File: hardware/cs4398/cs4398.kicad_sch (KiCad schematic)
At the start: 54 parts, among them J1 USB_C_Receptacle_USB2.0_16P, Q1 Si2323DS, U1 CS4398, U2 STM32H750IBKx, U3 TPS65131RGE, U4 USB3300-EZK, U5 TPS7A8300, U7 TPS60151DRV, Y1 CSTCE12M

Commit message: sync 9.15
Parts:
- removed R5: 1.5k, Resistor_SMD:R_0402_1005Metric, symbol Device:R
- added C1, C20: 10u, Capacitor_SMD:C_0805_2012Metric, symbol Device:C_Small
- added C16, C18, C21, C46, C47, C51, C52, C55, C56, C59, C6, C60, C64, C65, C66, C67, C68, C7, C71, C72, C73, C74, C77, C78, C79, C8: 100n, Capacitor_SMD:C_0402_1005Metric, symbol Device:C_Small
- added C19, C53, C54: 100u, Capacitor_Tantalum_SMD:CP_EIA-3528-15_AVX-H, symbol Device:C_Polarized_Small_US
- added C23, C4: 33u, Capacitor_Tantalum_SMD:CP_EIA-3528-15_AVX-H, symbol Device:C_Polarized_Small_US
- added C35, C41, C61, C75, C76: 100n, Capacitor_SMD:C_0603_1608Metric, symbol Device:C_Small
- added C44, C45: 6800p, Capacitor_SMD:C_0402_1005Metric, symbol Device:C_Small
- added C48, C49: 18n, Capacitor_SMD:C_0402_1005Metric, symbol Device:C_Small
- added C57, C58: 4700p, Capacitor_SMD:C_0402_1005Metric, symbol Device:C_Small
- added C62, C63: 1800p, Capacitor_SMD:C_0805_2012Metric, symbol Device:C_Small
- added C69, C70: 22u, Capacitor_Tantalum_SMD:CP_EIA-3528-15_AVX-H, symbol Device:C_Polarized_Small_US
- added C80, C81: 2.2u, Capacitor_SMD:C_0402_1005Metric, symbol Device:C_Small
- added F1: 1A, Fuse:Fuse_0603_1608Metric, symbol Device:Polyfuse
- added J2: GH1.25-4P, Connector_JST:JST_GH_BM04B-GHS-TBT_1x04-1MP_P1.25mm_Vertical, symbol Connector_Generic_MountingPin:Conn_01x04_MountingPin
- added Q2, Q3: S9012, Package_TO_SOT_SMD:SOT-23, symbol Transistor_BJT:MMBTA94
- added Q4, Q5: S9013, Package_TO_SOT_SMD:SOT-23, symbol Transistor_BJT:SS8050
- added R1, R11, R12, R13, R14: 10K, Resistor_SMD:R_0402_1005Metric, symbol Device:R
- added R10, R9: 2k, Resistor_SMD:R_0402_1005Metric, symbol Device:R
- added R15, R16: 1.5K, Resistor_SMD:R_0402_1005Metric, symbol Device:R
- added R20, R22, R37, R44, R45: 10k, Resistor_SMD:R_0603_1608Metric, symbol Device:R
- added R23, R25: 1.6k, Resistor_SMD:R_0402_1005Metric, symbol Device:R
- added R24, R26: 620, Resistor_SMD:R_0402_1005Metric, symbol Device:R
- added R27, R28, R30, R32: 270, Resistor_SMD:R_0402_1005Metric, symbol Device:R
- added R29, R31: 680, Resistor_SMD:R_0402_1005Metric, symbol Device:R
- added R33, R34: 100, Resistor_SMD:R_0603_1608Metric, symbol Device:R
- added R35, R36: 1.2k, Resistor_SMD:R_0402_1005Metric, symbol Device:R
- added R38, R39: 4.7K, Resistor_SMD:R_0603_1608Metric, symbol Device:R
- added R40, R41: 100k, Resistor_SMD:R_0402_1005Metric, symbol Device:R
- added R42, R43: 560, Resistor_SMD:R_0402_1005Metric, symbol Device:R
- added R46: 10k, Resistor_SMD:R_0402_1005Metric, symbol Device:R
- added R7, R8: 5.1k, Resistor_SMD:R_0402_1005Metric, symbol Device:R
- added SW1, SW2, SW3, SW4: SW_Omron_B3FS, Button_Switch_SMD:SW_SPST_TS-1088-xR025, symbol Switch:SW_Omron_B3FS
- added U6: OPA1612AxD, Package_SON:WSON-8-1EP_3x3mm_P0.5mm_EP1.2x2mm_ThermalVias, symbol Amplifier_Operational:OPA1612AxD
- added Y2: CSTCE24M, Crystal:Resonator_SMD_Murata_CSTxExxV-3Pin_3.0x1.1mm, symbol Device:Crystal_GND2_Small
- C22: renamed from C13; footprint Capacitor_SMD:C_0402_1005Metric -> Capacitor_SMD:C_0805_2012Metric
- Y1: value CSTCE12M -> CSTCE24M
- renumbered C22 to C11, C11 to C12, C28 to C13, C21 to C14, C23 to C15, C24 to C17, C4 to C2, C7 to C24, C6 to C25, C12 to C26, C5 to C27, C14 to C28, C2 to C29, C9 to C3, C20 to C30, C19 to C31, C25 to C32, C17 to C33, C1 to C34, C42 to C36, C16 to C37, C29 to C38, C15 to C39, C18 to C40, C26 to C42, C30 to C43, C8 to C5, C27 to C50, C3 to C9, R9 to R17, R10 to R18, R7 to R19, R1 to R2, R8 to R21, R2 to R3, R6 to R4, R4 to R5, R3 to R6, U7 to U1, U5 to U2, U1 to U3, U3 to U4, U4 to U5, U2 to U7
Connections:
- net +15V: now also C68.2, U6.8 (V+)
- net +3.3V: now also U3.12 (AD0/~{CS}), U3.14 (VLC), U3.27 (VLS), U3.7 (VD), U7.C6 (PDR_ON), U7.P1 (VREF+), C1.1, C35.1, C46.1, C47.1, C51.1, C52.1, C55.1, C56.1, C59.1, C6.1, C60.1, C64.1, C65.1, C66.1, C67.1, C7.1, C71.1, C72.1, C73.1, C74.1, C77.1, C78.1, C8.1, F1.2, R1.2, R22.2, R37.2, R38.1, R44.2, R45.2
- net +5V: now also U3.17 (VREF), U3.22 (VA), C16.1, C18.1, C20.1, C23.1, Q2.2 (E), Q3.2 (E), R11.1, R12.1
- net -15V: now also C79.2, U6.4 (V-), U6.9 (EP)
- net GND: now also U3.1 (DSD_B), U3.11 (SDA/CDOUT), U3.16 (REF_GND), U3.2 (DSD_SCLK), U3.21 (AGND), U3.28 (DSD_A), U3.8 (DGND), U3.9 (AD1/CDIN), U7.N1 (VREF-), C1.2, C16.2, C18.2, C19.2, C20.2, C21.2, C23.2, C4.2, C41.1, C44.2, C45.2, C46.2, C47.2, C48.2, C49.2, C51.2, C52.2, C53.2, C54.2, C55.2, C56.2, C57.2, C58.2, C59.2, C6.2, C60.2, C61.1, C64.2, C65.2, C66.2, C67.2, C68.1, C7.2, C71.2, C72.2, C73.2, C74.2, C75.1, C76.1, C77.2, C78.2, C79.1, C8.2, C80.2, C81.2, J2.3 (Pin_3), J2.MP (MountPin), Q4.2 (E), Q5.2 (E), R13.2, R14.2, R20.2, R39.1, R40.2, R41.2, R46.1, R7.2, R8.2, SW1.2, SW2.2, SW3.2, SW4.2, Y2.2
- net SCLK: now reaches U7.A10 (PB3)
- net SCLK: now also U3.4 (SCLK)
- net SDATA: now reaches U7.A11 (PD7)
- net SDATA: now also U3.3 (SDIN)
- net LRCK: now reaches U7.A13 (PA15)
- net LRCK: now also U3.5 (LRCK)
- net CLK: now reaches U7.A14 (PA14)
- net CLK: now also R34.2, R39.2
- net DIO: now reaches U7.A15 (PA13)
- net DIO: now also R33.2, R38.2
- net D7: now reaches U7.A6 (PB5)
- net D7: now also U5.17 (DATA7)
- net SW2: now reaches U7.D1 (PC13)
- net SW2: now also C76.2, R45.1, SW4.1
- net at U7.D6 (BOOT0): now also R46.2
- net DIR: now reaches U7.E4 (PI11)
- net DIR: now also U5.12 (DIR)
- net at U7.F13 (VCAP): now also C80.1
- net SW3: now reaches U7.F15 (PA8)
- net SW3: now also C75.2, R44.1, SW3.1
- net at U7.G1 (PH0): now also Y2.1
- net at U7.H1 (PH1): now also Y2.3
- net NXT: now reaches U7.H4 (PH4)
- net NXT: now also U5.11 (NXT)
- net RS: now reaches U7.J1 (NRST)
- net RS: now also C41.2, R22.1, SW1.1
- net at U7.M10 (VCAP): now also C81.1
- net STP: now reaches U7.M2 (PC0)
- net STP: now also U5.13 (STP)
- net SW1: now reaches U7.N15 (PD10)
- net SW1: now also C61.2, R37.1, SW2.1
- net MCLK: now reaches U7.N5 (PC4)
- net MCLK: now also U3.6 (MCLK)
- net D5: now reaches U7.P12 (PB12)
- net D5: now also U5.19 (DATA5)
- net D6: now reaches U7.P13 (PB13)
- net D6: now also U5.18 (DATA6)
- net USB_RS: now reaches U7.P15 (PD8)
- net USB_RS: now also U5.9 (RESET), C35.2, R20.1
- net CK: now reaches U7.P4 (PA5)
- net CK: now also U5.14 (CLKOUT)
- net D3: now reaches U7.R12 (PB10)
- net D3: now also U5.21 (DATA3)
- net D4: now reaches U7.R13 (PB11)
- net D4: now also U5.20 (DATA4)
- net D0: now reaches U7.R2 (PA3)
- net D0: now also U5.24 (DATA0)
- net D2: now reaches U7.R4 (PB1)
- net D2: now also U5.22 (DATA2)
- net D1: now reaches U7.R5 (PB0)
- net D1: now also U5.23 (DATA1)
- net DEM: now reaches U3.10 (SCL/CCLK)
- net at U3.13 (~{RST}): now also C4.1, R1.1
- net at U3.15 (FILT+): now also C19.1, C21.1
- net RMUTE: now reaches U3.18 (BMUTEC)
- net RMUTE: now also R10.2, R8.1
- net ROUT-: now reaches U3.19 (AOUTB-)
- net ROUT-: now also R24.2
- net ROUT+: now reaches U3.20 (AOUTB+)
- net ROUT+: now also R23.2
- net LOUT+: now reaches U3.23 (AOUTA+)
- net LOUT+: now also R25.2
- net LOUT-: now reaches U3.24 (AOUTA-)
- net LOUT-: now also R26.2
- net LMUTE: now reaches U3.25 (AMUTEC)
- net LMUTE: now also R7.1, R9.2
- new net: C49.1, R26.1, R28.1, R32.2
- new net: C45.1, R25.1, R31.2, R36.2
- new net: C48.1, R24.1, R27.1, R30.2
- new net: C58.1, R32.1, U6.6 (-)
- new net: C63.1, R31.1, U6.5 (+)
- new net: C44.1, R23.1, R29.2, R35.2
- new net: Q2.1 (B), R11.2, R9.1
- new net: Q4.1 (B), R15.1
- new net: Q5.1 (B), R16.1
- new net: J2.1 (Pin_1), R33.1
- new net: J2.2 (Pin_2), R34.1
- new net: F1.1, J2.4 (Pin_4)
- new net: C53.1, R27.2
- new net: C69.2, R40.1, R42.2
- new net: C63.2, C70.1, R36.1, U6.7
- new net: C70.2, R41.1, R43.2
- new net: C57.1, R30.1, U6.2 (-)
- new net: Q3.3 (C), R14.1, R16.2
- new net: C62.1, R29.1, U6.3 (+)
- new net: Q2.3 (C), R13.1, R15.2
- new net: C54.1, R28.2
- new net: Q3.1 (B), R10.1, R12.2
- new net: C62.2, C69.1, R35.1, U6.1
- new net LOUT: Q4.3 (C), R43.1
- new net ROUT: Q5.3 (C), R42.1
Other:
- moved on the sheet: C10, C11, C12, C13, C14, C15, C17, C2, C22, C26, C28, C3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

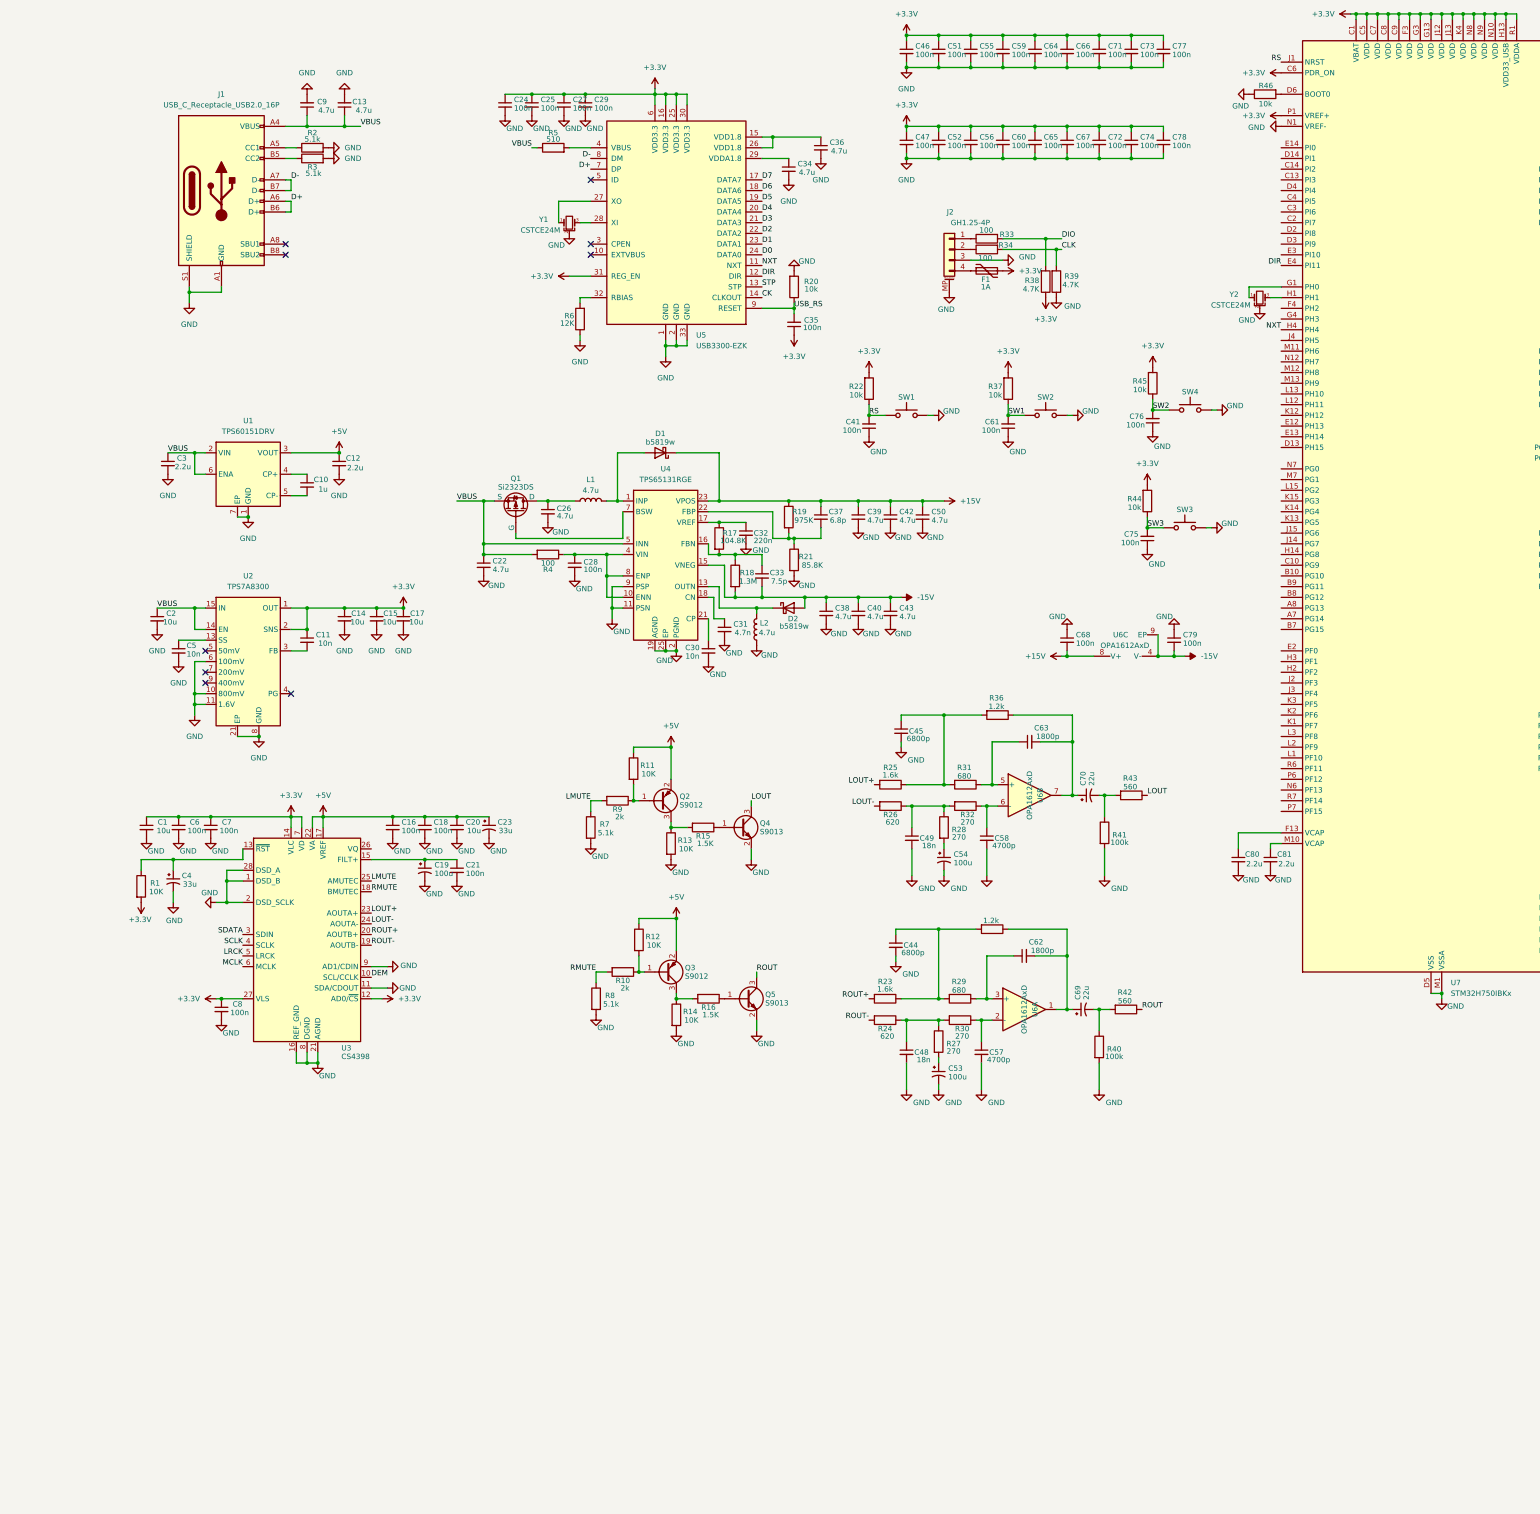
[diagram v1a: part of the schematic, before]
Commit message: 添加4.4mm平衡输出
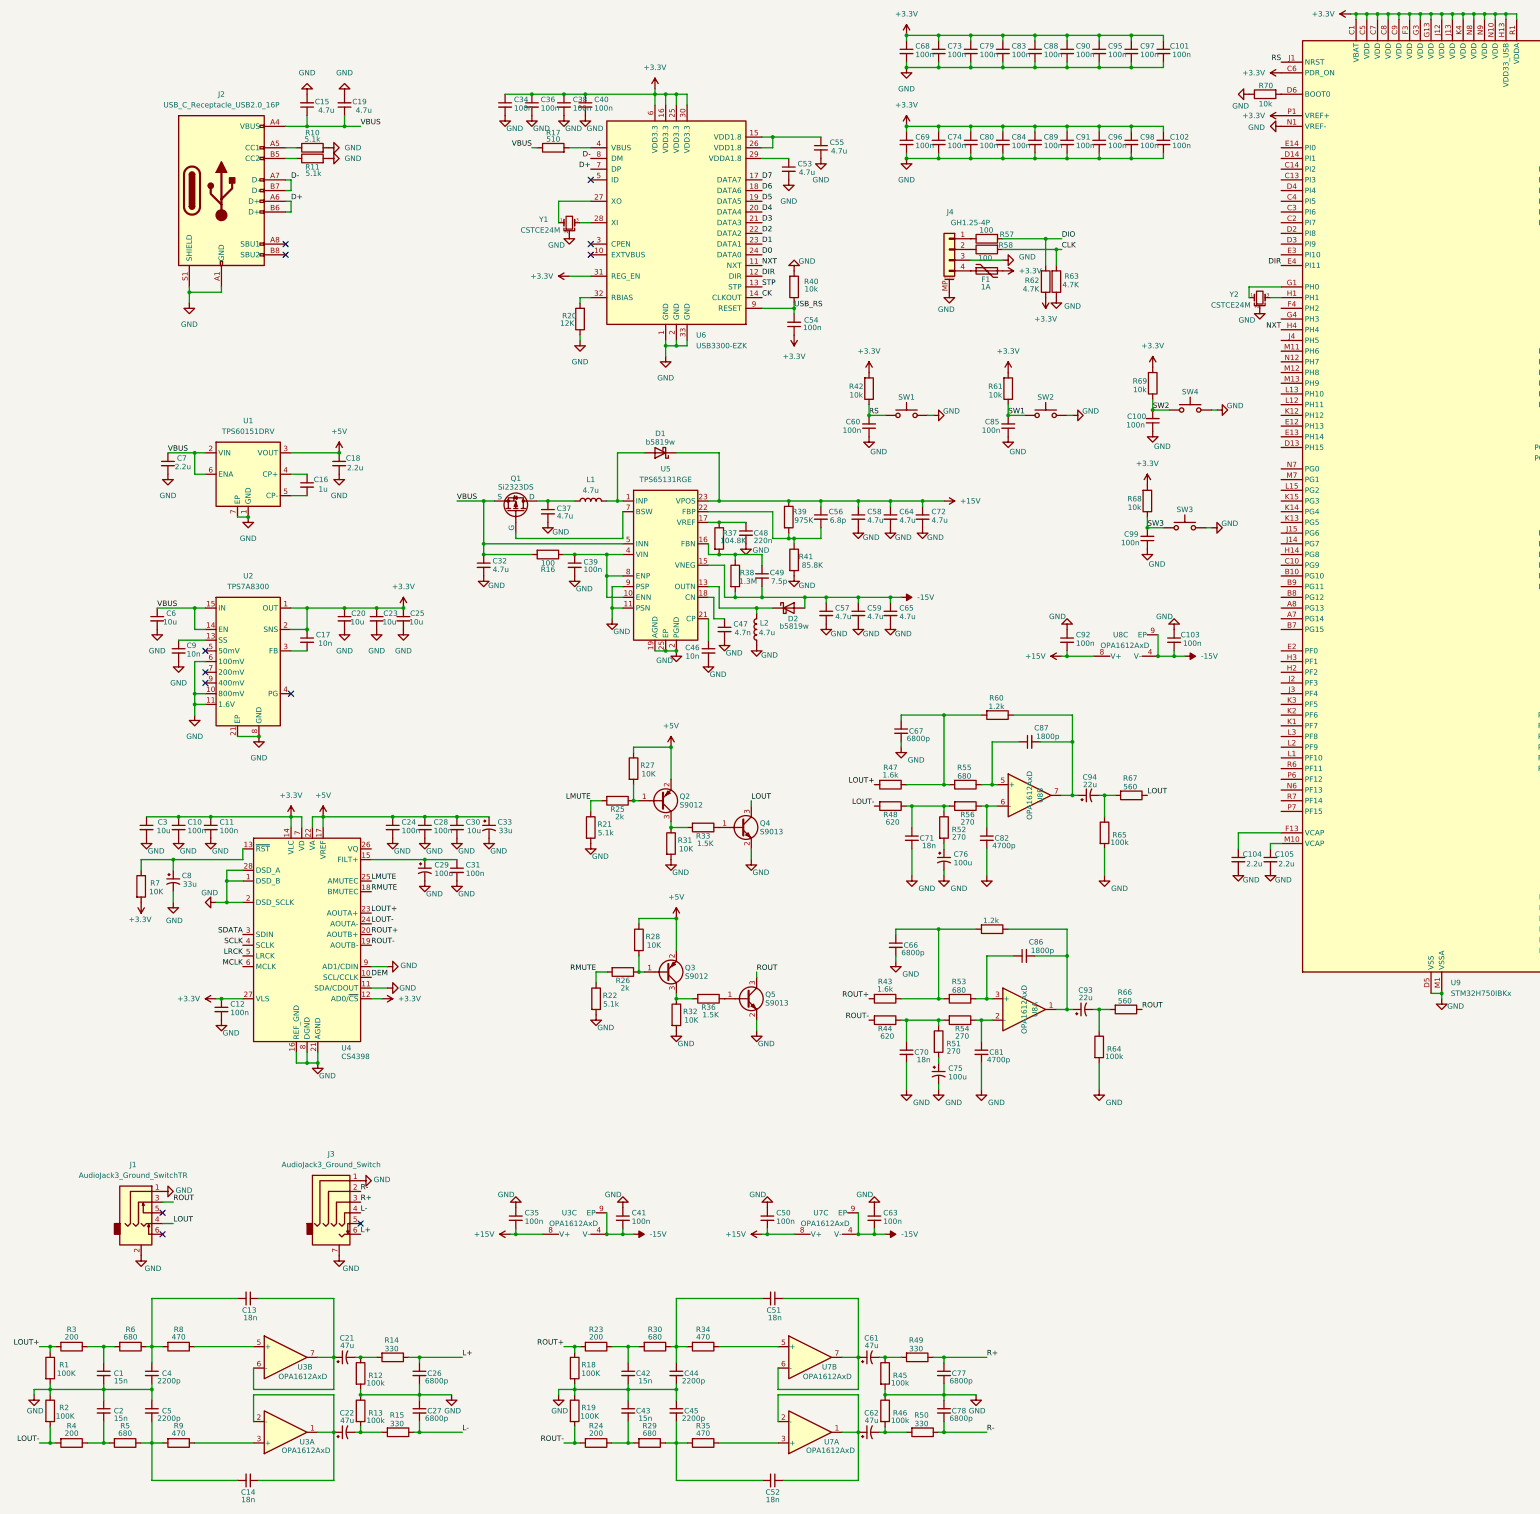
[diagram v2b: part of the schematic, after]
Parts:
- added C1, C2, C42, C43: 15n, Capacitor_SMD:C_0402_1005Metric, symbol Device:C_Small
- added C13, C14, C51, C52: 18n, Capacitor_SMD:C_0402_1005Metric, symbol Device:C_Small
- added C21, C22, C61, C62: 47u, Capacitor_Tantalum_SMD:CP_EIA-3528-15_AVX-H, symbol Device:C_Polarized_Small_US
- added C26, C27, C77, C78: 6800p, Capacitor_SMD:C_0402_1005Metric, symbol Device:C_Small
- added C35, C41, C50, C63: 100n, Capacitor_SMD:C_0402_1005Metric, symbol Device:C_Small
- added C4, C44, C45, C5: 2200p, Capacitor_SMD:C_0402_1005Metric, symbol Device:C_Small
- added J1: AudioJack3_Ground_SwitchTR, Connector_Audio:Jack_3.5mm_PJ311_Horizontal, symbol Connector_Audio:AudioJack3_Ground_SwitchTR
- added J3: AudioJack3_Ground_Switch, Connector_Audio:Jack_6.35mm_Neutrik_NSJ12HH-1_Horizontal, symbol Connector_Audio:AudioJack3_Ground_Switch
- added R1, R18, R19, R2: 100K, Resistor_SMD:R_0402_1005Metric, symbol Device:R
- added R12, R13, R45, R46: 100k, Resistor_SMD:R_0402_1005Metric, symbol Device:R
- added R14, R15, R49, R50: 330, Resistor_SMD:R_0402_1005Metric, symbol Device:R
- added R23, R24, R3, R4: 200, Resistor_SMD:R_0402_1005Metric, symbol Device:R
- added R29, R30, R5, R6: 680, Resistor_SMD:R_0402_1005Metric, symbol Device:R
- added R34, R35, R8, R9: 470, Resistor_SMD:R_0402_1005Metric, symbol Device:R
- added U3, U7: OPA1612AxD, Package_SON:WSON-8-1EP_3x3mm_P0.5mm_EP1.2x2mm_ThermalVias, symbol Amplifier_Operational:OPA1612AxD
- C86: renamed from C62; footprint Capacitor_SMD:C_0805_2012Metric -> Capacitor_SMD:C_0402_1005Metric
- C87: renamed from C63; footprint Capacitor_SMD:C_0805_2012Metric -> Capacitor_SMD:C_0402_1005Metric
- renumbered C6 to C10, C76 to C100, C77 to C101, C78 to C102, C79 to C103, C80 to C104, C81 to C105, C7 to C11, C8 to C12, C9 to C15, C10 to C16, C11 to C17, C12 to C18, C13 to C19, C14 to C20, C15 to C23, C16 to C24, C17 to C25, C18 to C28, C19 to C29, C1 to C3, C20 to C30, C21 to C31, C22 to C32, C23 to C33, C24 to C34, C25 to C36, C26 to C37, C27 to C38, C28 to C39, C29 to C40, C30 to C46, C31 to C47, C32 to C48, C33 to C49, C34 to C53, C35 to C54, C36 to C55, C37 to C56, C38 to C57, C39 to C58, C40 to C59, C2 to C6, C41 to C60, C42 to C64, C43 to C65, C44 to C66, C45 to C67, C46 to C68, C47 to C69, C3 to C7, C48 to C70, C49 to C71, C50 to C72, C51 to C73, C52 to C74, C53 to C75, C54 to C76, C55 to C79, C4 to C8, C56 to C80, C57 to C81, C58 to C82, C59 to C83, C60 to C84, C61 to C85, C64 to C88, C65 to C89, C5 to C9, C66 to C90, C67 to C91, C68 to C92, C69 to C93, C70 to C94, C71 to C95, C72 to C96, C73 to C97, C74 to C98, C75 to C99, J1 to J2, J2 to J4, R2 to R10, R3 to R11, R4 to R16, R5 to R17, R6 to R20, R7 to R21, R8 to R22, R9 to R25, R10 to R26, R11 to R27, R12 to R28, R13 to R31, R14 to R32, R15 to R33, R16 to R36, R17 to R37, R18 to R38, R19 to R39, R20 to R40, R21 to R41, R22 to R42, R23 to R43, R24 to R44, R25 to R47, R26 to R48, R27 to R51, R28 to R52, R29 to R53, R30 to R54, R31 to R55, R32 to R56, R33 to R57, R34 to R58, R35 to R59, R36 to R60, R37 to R61, R38 to R62, R39 to R63, R40 to R64, R41 to R65, R42 to R66, R43 to R67, R44 to R68, R45 to R69, R1 to R7, R46 to R70, U3 to U4, U4 to U5, U5 to U6, U6 to U8, U7 to U9
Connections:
- net +15V: now also C35.2, C50.2, U3.8 (V+), U7.8 (V+)
- net -15V: now also C41.2, C63.2, U3.4 (V-), U3.9 (EP), U7.4 (V-), U7.9 (EP)
- net GND: now also C1.2, C2.1, C26.2, C27.1, C35.1, C4.2, C41.1, C42.2, C43.1, C44.2, C45.1, C5.1, C50.1, C63.1, C77.2, C78.1, J1.1, J1.2, J3.1, J3.7, R1.2, R12.2, R13.1, R18.2, R19.1, R2.1, R45.2, R46.1
- net LOUT: now also J1.4
- net LOUT+: now also R1.1, R3.2
- net LOUT-: now also R2.2, R4.2
- net ROUT: now also J1.3
- net ROUT+: now also R18.1, R23.2
- net ROUT-: now also R19.2, R24.2
- new net: C62.2, R46.2, R50.2
- new net: R35.1, U7.3 (+)
- new net: C45.2, C52.2, R29.1, R35.2
- new net: C43.2, R24.1, R29.2
- new net: C44.1, C51.2, R30.1, R34.2
- new net: C42.1, R23.1, R30.2
- new net: C61.2, R45.1, R49.2
- new net: C14.1, C22.1, U3.1, U3.2 (-)
- new net: C22.2, R13.2, R15.2
- new net: C14.2, C5.2, R5.1, R9.2
- new net: C2.2, R4.1, R5.2
- new net: C51.1, C61.1, U7.6 (-), U7.7
- new net: R8.1, U3.5 (+)
- new net: C13.1, C21.1, U3.6 (-), U3.7
- new net: R9.1, U3.3 (+)
- new net: C21.2, R12.1, R14.2
- new net: C52.1, C62.1, U7.1, U7.2 (-)
- new net: R34.1, U7.5 (+)
- new net: C13.2, C4.1, R6.1, R8.2
- new net: C1.1, R3.1, R6.2
- new net L+: C26.1, J3.6, R14.1
- new net L-: C27.2, J3.4, R15.1
- new net R+: C77.1, J3.3, R49.1
- new net R-: C78.2, J3.2, R50.1
- no-connect marks 9 -> 12
